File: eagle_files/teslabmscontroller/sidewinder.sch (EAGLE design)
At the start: 42 parts, among them J1 TERMINAL12, J2 TERMINAL12, Q1 2N3704, Q2 2N3906, T1 V_REG_317SINK, U1 G3VM41, U2 G3VM41, U3 G3VM41, U4 SN65HVD230, U5 SP720APP, U6 SP720APP

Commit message: run and charging to zener
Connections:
- removed net N$2: B1.A5/19/SCL0, C9.1, R12.2, R16.1
- new net RUN_SW: J1.J8, R16.2
- net CHARGING: now also U5.IN9
- net RUN: now also B1.A5/19/SCL0, C9.1, R12.2, R16.1, U5.IN12; no longer J1.J8, R16.2

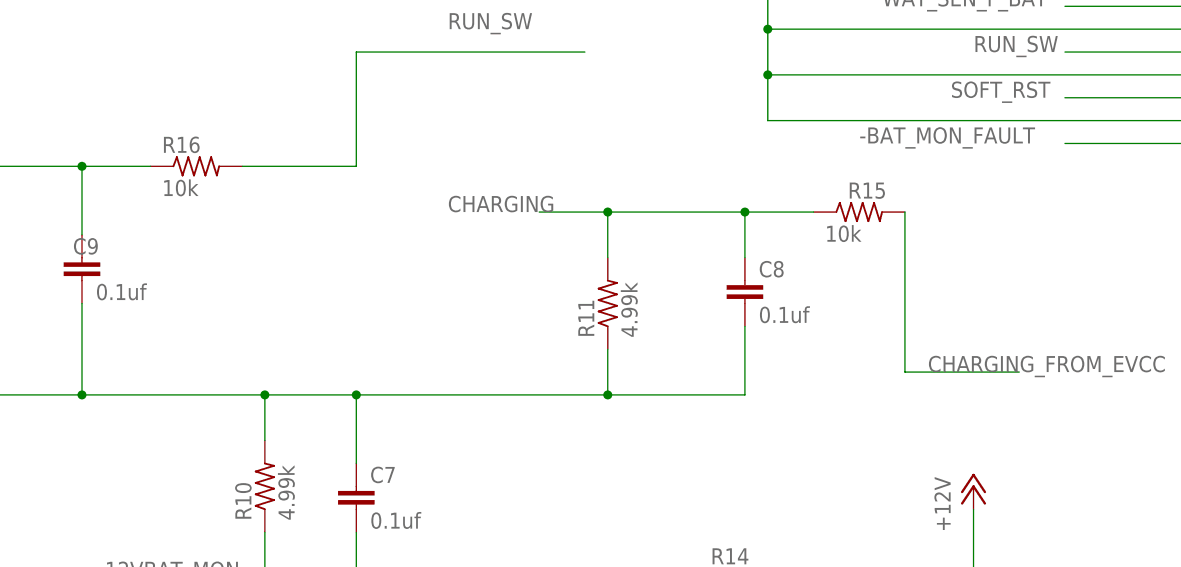
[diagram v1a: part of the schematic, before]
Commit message: adjusted 12Vto5V deviders
changed 2 resistors from 10k to 15k after we fried a board...
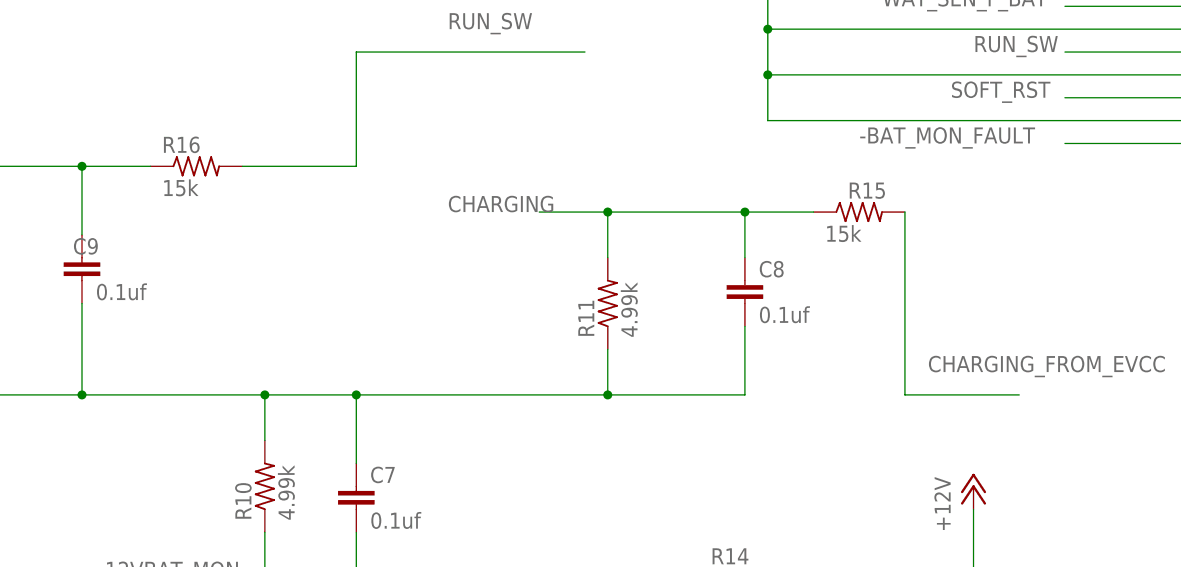
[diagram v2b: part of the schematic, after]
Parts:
- R15, R16: value 10k -> 15k
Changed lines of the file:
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@@
 <part name="GND3" library="supply1" library_urn="urn:adsk.eagle:library:371" deviceset="GND" device=""/>
 <part name="R12" library="rcl" library_urn="urn:adsk.eagle:library:334" deviceset="R-US_" device="0207/10" package3d_urn="urn:adsk.eagle:package:23491/2" value="4.99k"/>
-<part name="R16" library="rcl" library_urn="urn:adsk.eagle:library:334" deviceset="R-US_" device="0207/10" package3d_urn="urn:adsk.eagle:package:23491/2" value="10k"/>
+<part name="R16" library="rcl" library_urn="urn:adsk.eagle:library:334" deviceset="R-US_" device="0207/10" package3d_urn="urn:adsk.eagle:package:23491/2" value="15k"/>
 <part name="GND4" library="supply1" library_urn="urn:adsk.eagle:library:371" deviceset="GND" device=""/>
-<part name="R15" library="rcl" library_urn="urn:adsk.eagle:library:334" deviceset="R-US_" device="0207/10" package3d_urn="urn:adsk.eagle:package:23491/2" value="10k"/>
+<part name="R15" library="rcl" library_urn="urn:adsk.eagle:library:334" deviceset="R-US_" device="0207/10" package3d_urn="urn:adsk.eagle:package:23491/2" value="15k"/>
 <part name="R11" library="rcl" library_urn="urn:adsk.eagle:library:334" deviceset="R-US_" device="0207/10" package3d_urn="urn:adsk.eagle:package:23491/2" value="4.99k"/>
 <part name="R14" library="rcl" library_urn="urn:adsk.eagle:library:334" deviceset="R-US_" device="0207/10" package3d_urn="urn:adsk.eagle:package:23491/2" value="20k"/>
@@
 <segment>
 <pinref part="R15" gate="G$1" pin="2"/>
-<wire x1="223.52" y1="91.44" x2="223.52" y2="73.66" width="0.1524" layer="91"/>
-<wire x1="223.52" y1="73.66" x2="236.22" y2="73.66" width="0.1524" layer="91"/>
+<wire x1="223.52" y1="91.44" x2="223.52" y2="71.12" width="0.1524" layer="91"/>
+<wire x1="223.52" y1="71.12" x2="236.22" y2="71.12" width="0.1524" layer="91"/>
 <label x="226.06" y="73.66" size="1.778" layer="95"/>
 </segment>
